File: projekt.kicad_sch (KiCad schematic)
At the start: 117 parts, among them IC1 DW01+G, IC4 MIC5504-3.3YM5-TR, J1 10118194-0001LF, J10 Conn_01x06_Pin, J2 TP4056, J4 Conn_01x02_Socket, Q1 AO3420, Q2 AO3420, Q3 AO3420, Q4 AO3420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

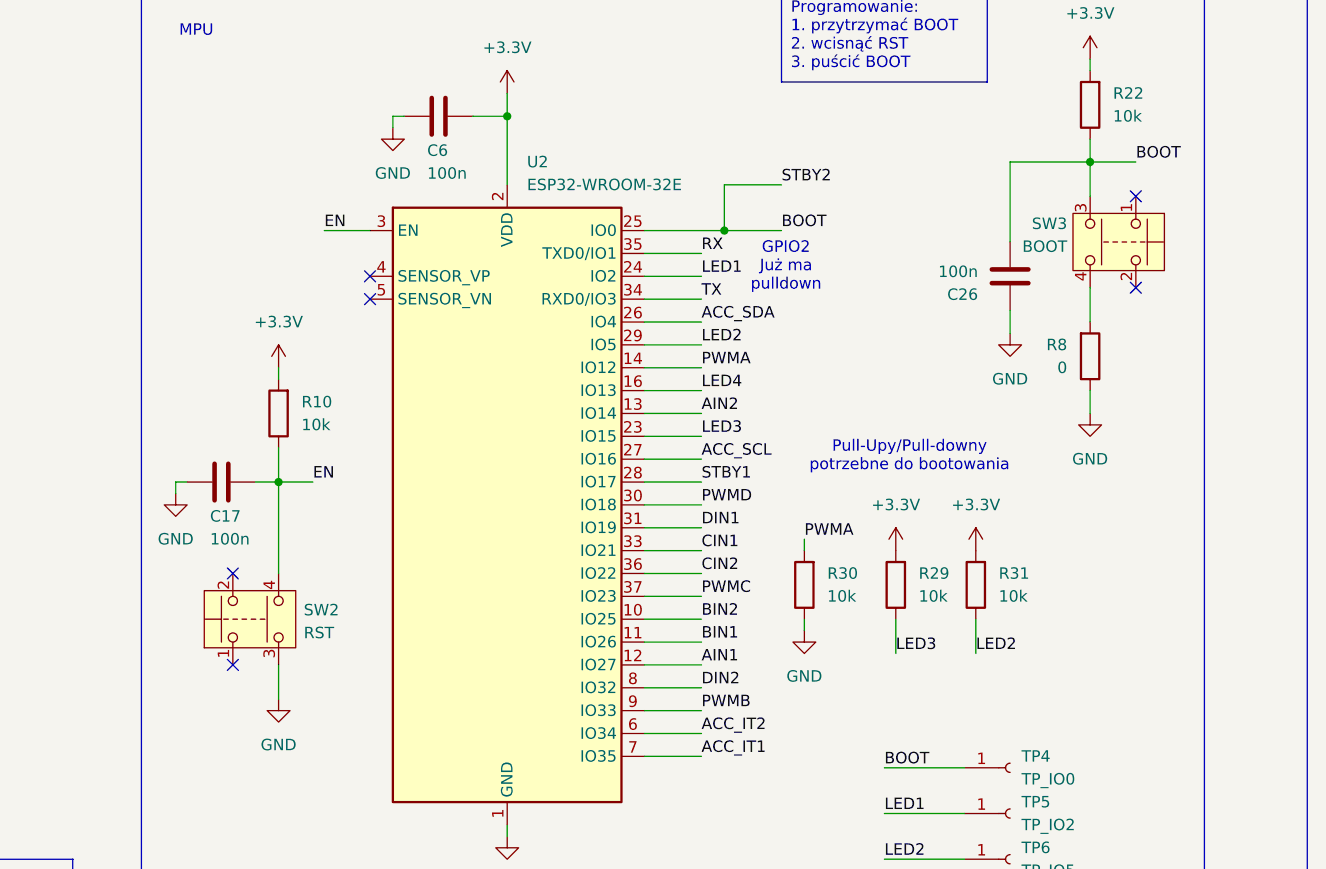
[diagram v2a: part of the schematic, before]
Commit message: Podmiana przycisków
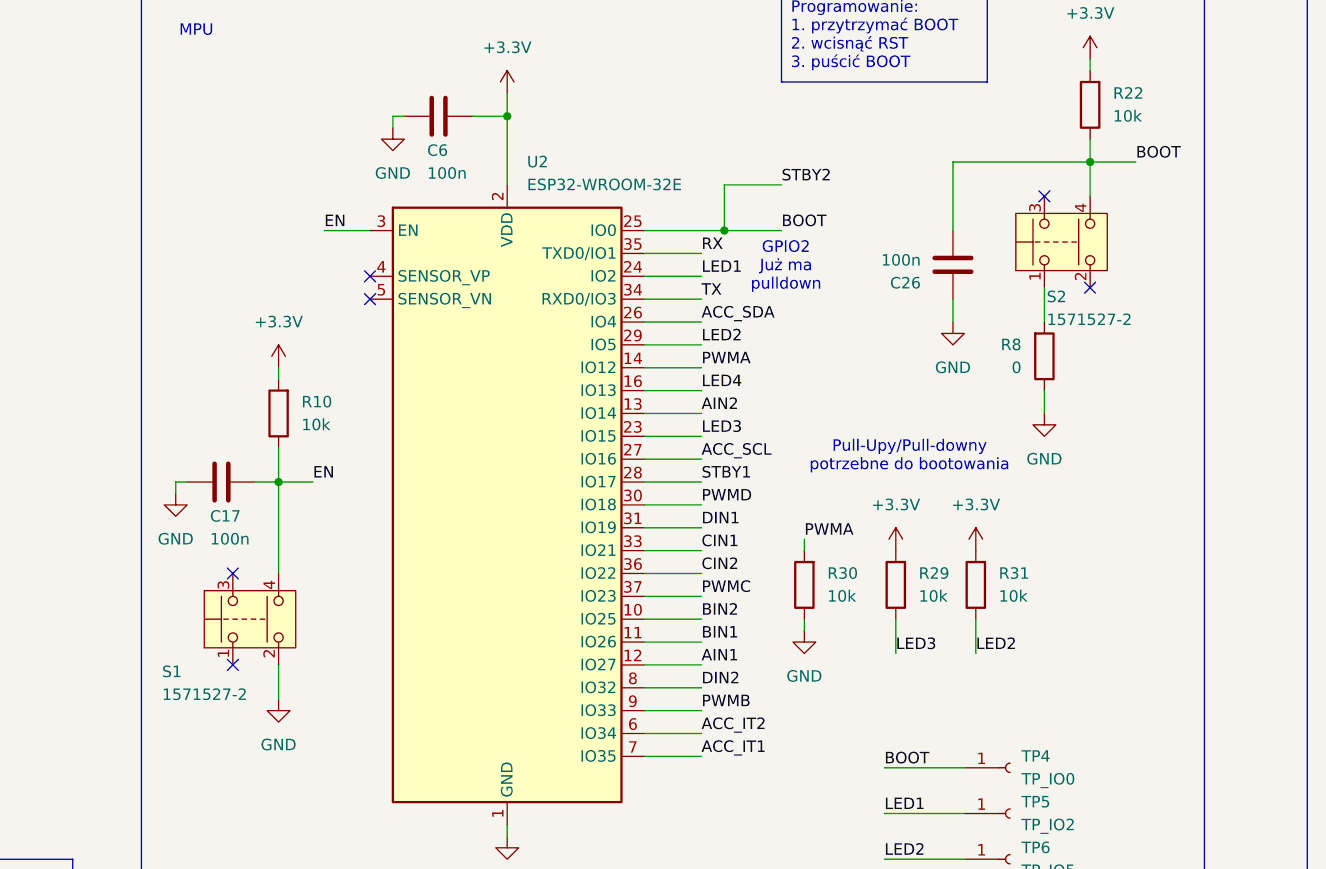
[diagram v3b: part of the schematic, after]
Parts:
- removed SW2: RST, Button_Switch_SMD:TSS 62 N, symbol Switch:SW_Push_Dual
- removed SW3: BOOT, Button_Switch_SMD:TSS 62 N, symbol Switch:SW_Push_Dual
- added S1, S2: 1571527-2, 15715272, symbol Switch:SW_Push_Dual
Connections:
- net BOOT: now also S2.4
- net EN: now also S1.4
- net GND: now also S1.2
- net at R8.2: now also S2.1
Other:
- moved on the sheet: C26, R8

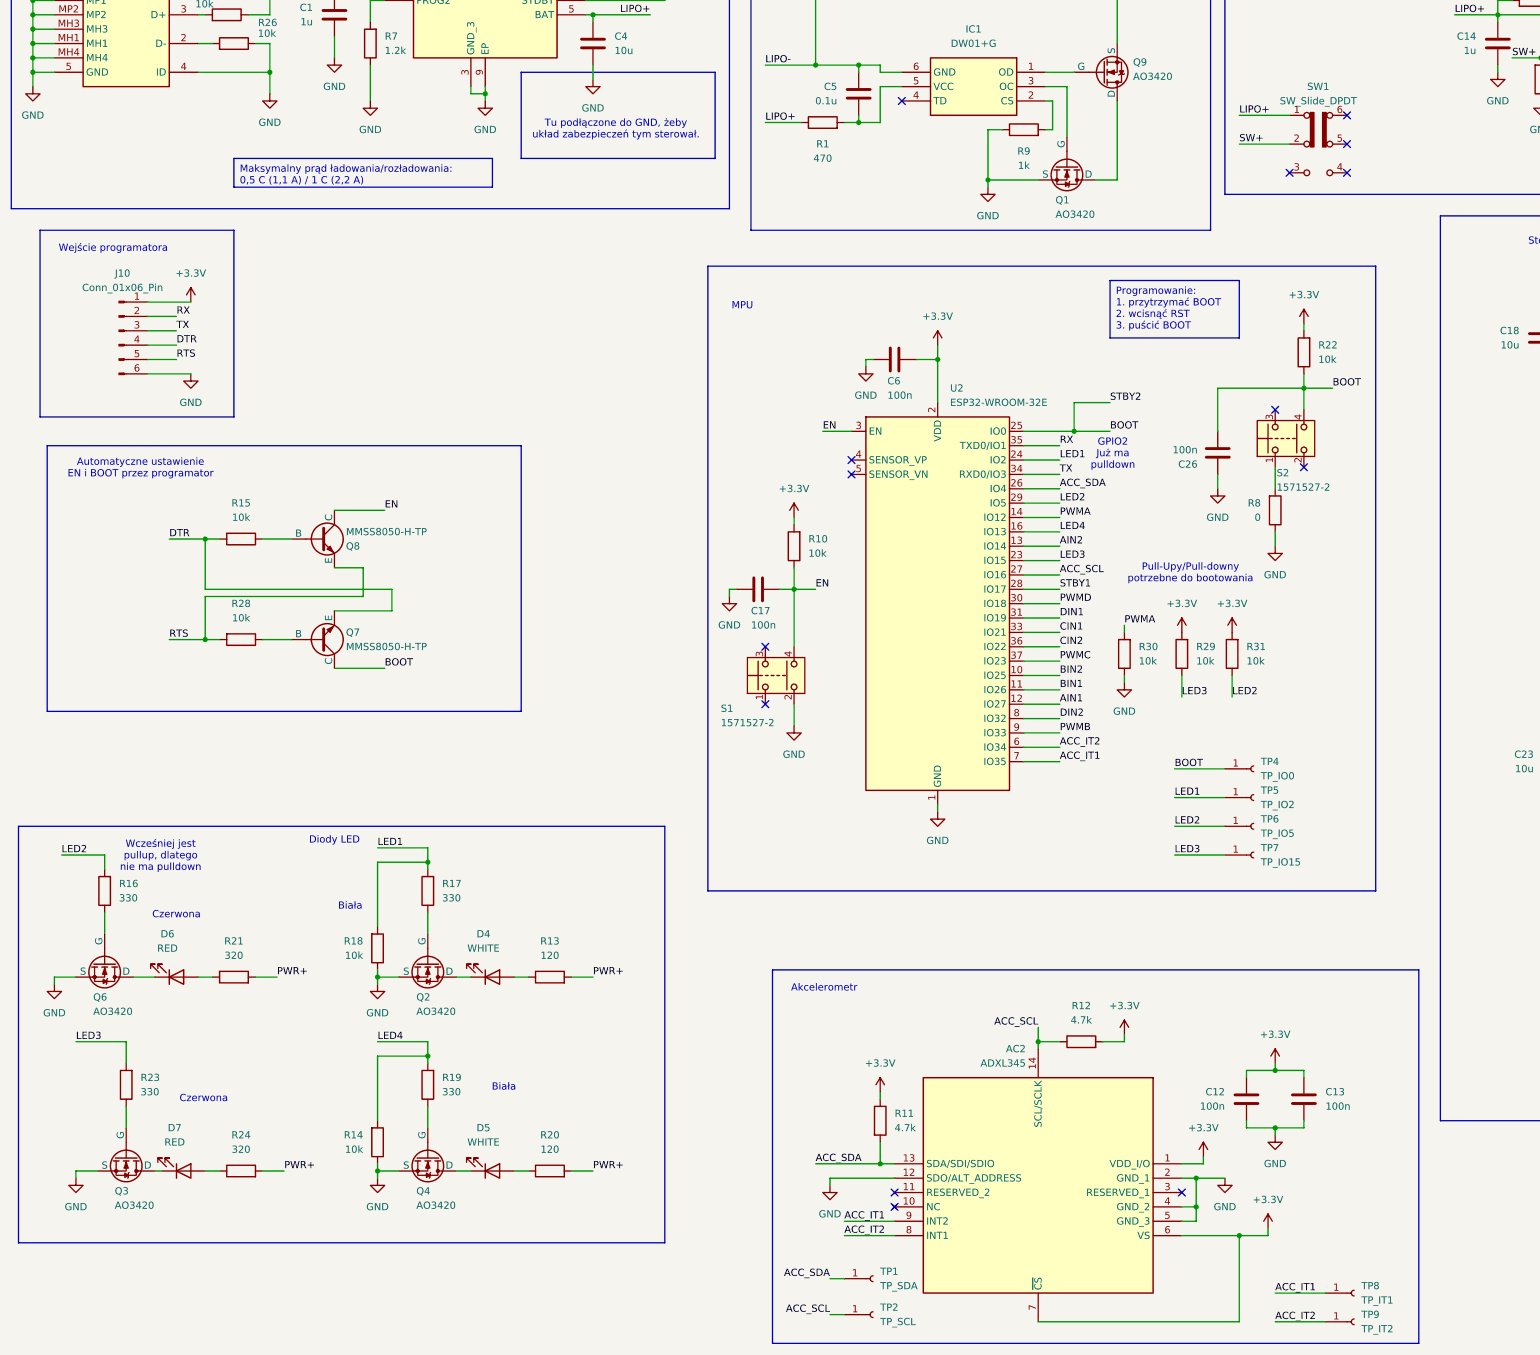
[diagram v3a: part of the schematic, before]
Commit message: Podmiana esp32 i footprinta switcha
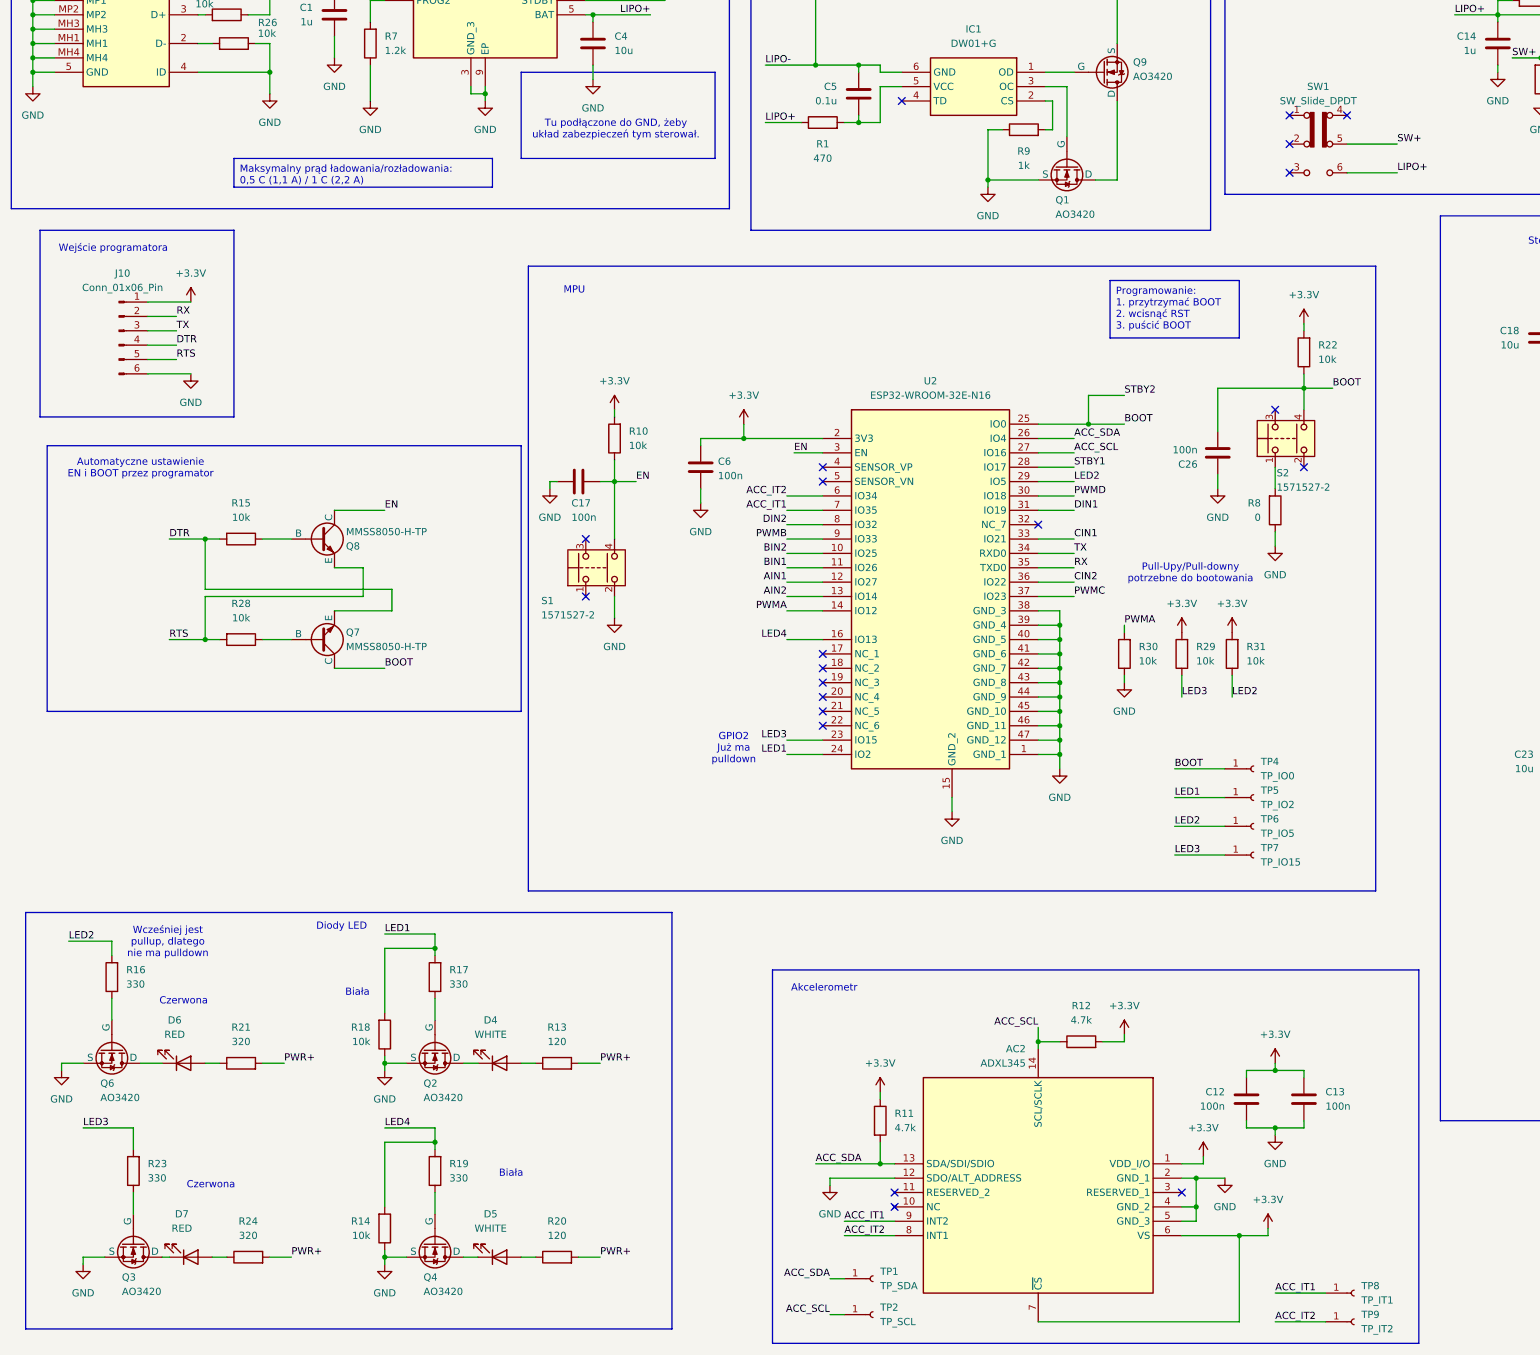
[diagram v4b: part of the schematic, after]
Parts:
- removed U2: ESP32-WROOM-32E, RF_Module:ESP32-WROOM-32D, symbol RF_Module:ESP32-WROOM-32E
- added U2: ESP32-WROOM-32E-N16, ESP32WROOM32EN16, symbol SamacSys_Parts:ESP32-WROOM-32E-N16
- SW1: footprint Button_Switch_THT:SW_CK_JS202011AQN_DPDT_Angled -> Button_Switch_THT:SS22T20
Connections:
- net +3.3V: now also U2.2 (3V3)
- net ACC_IT1: now also U2.7 (IO35)
- net ACC_IT2: now also U2.6 (IO34)
- net ACC_SCL: now also U2.27 (IO16)
- net ACC_SDA: now also U2.26 (IO4)
- net AIN1: now also U2.12 (IO27)
- net AIN2: now also U2.13 (IO14)
- net BIN1: now also U2.11 (IO26)
- net BIN2: now also U2.10 (IO25)
- net BOOT: now also U2.25 (IO0)
- net CIN1: now also U2.33 (IO21)
- net CIN2: now also U2.36 (IO22)
- net DIN1: now also U2.31 (IO19)
- net DIN2: now also U2.8 (IO32)
- net EN: now also U2.3 (EN)
- net GND: now also U2.1 (GND_1), U2.15 (GND_2), U2.38 (GND_3), U2.39 (GND_4), U2.40 (GND_5), U2.41 (GND_6), U2.42 (GND_7), U2.43 (GND_8), U2.44 (GND_9), U2.45 (GND_10), U2.46 (GND_11), U2.47 (GND_12)
- net LED1: now also U2.24 (IO2)
- net LED2: now also U2.29 (IO5)
- net LED3: now also U2.23 (IO15)
- net LED4: now also U2.16 (IO13)
- net LIPO+: now also SW1.6 (C); no longer SW1.1 (A)
- net PWMA: now also U2.14 (IO12)
- net PWMB: now also U2.9 (IO33)
- net PWMC: now also U2.37 (IO23)
- net PWMD: now also U2.30 (IO18)
- net RX: now also U2.35 (TXD0)
- net STBY1: now also U2.28 (IO17)
- net SW+: now also SW1.5 (B); no longer SW1.2 (B)
- net TX: now also U2.34 (RXD0)
- no-connect marks 15 -> 22
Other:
- moved on the sheet: C17, C6, D4, D5, D6, D7, Q2, Q3, Q4, Q6, R10, R13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

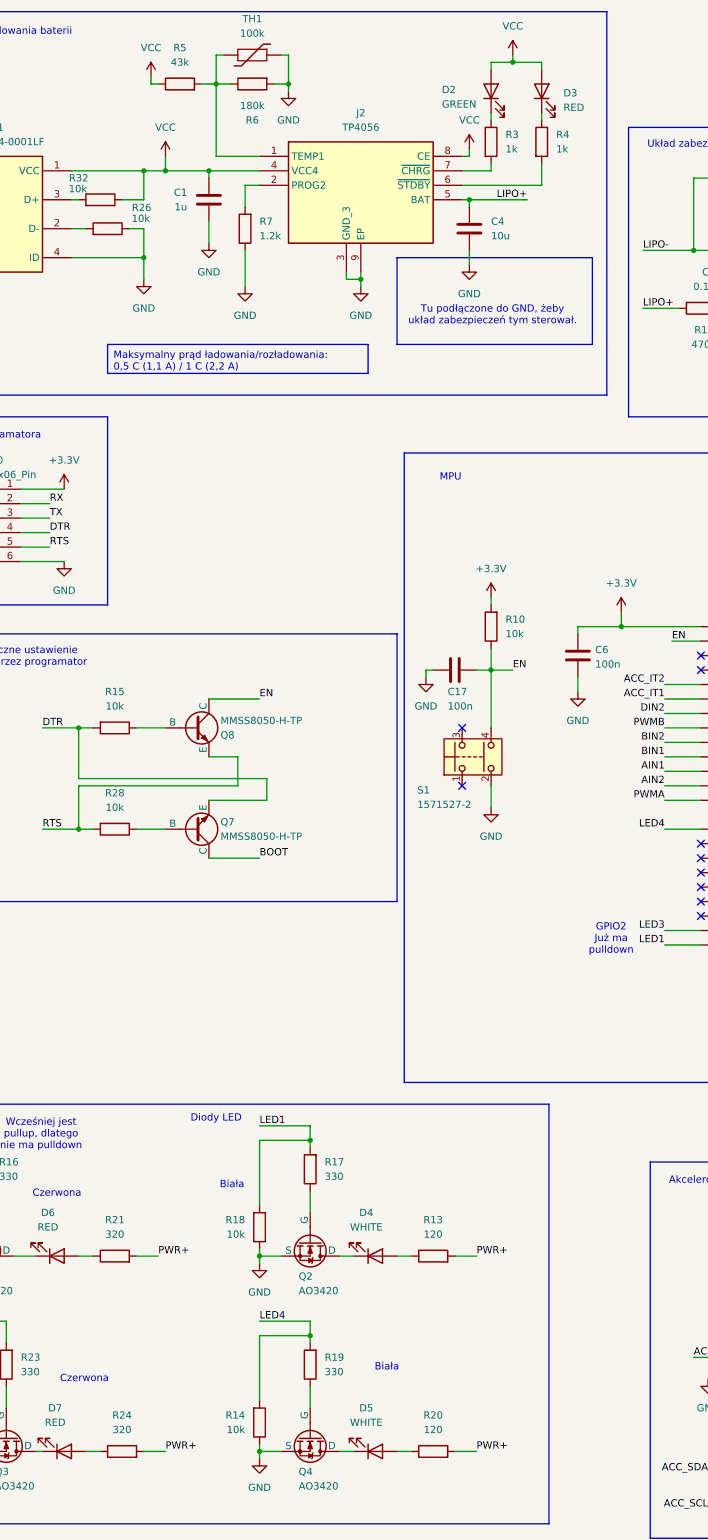
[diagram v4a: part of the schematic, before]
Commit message: Podmiana ścieżek na plane w dolnych wyjściach silników
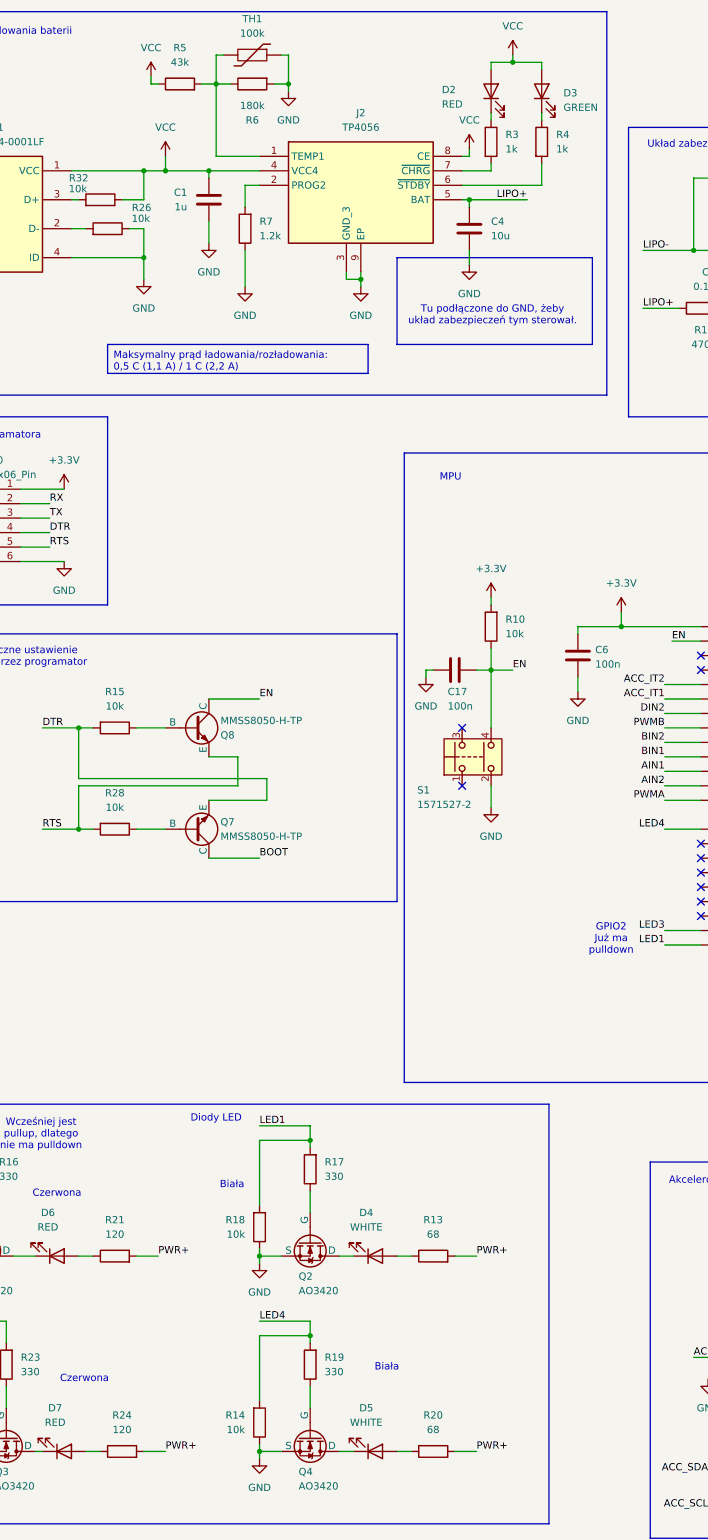
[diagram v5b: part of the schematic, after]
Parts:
- D2: value GREEN -> RED
- D3: value RED -> GREEN
- R13, R20: value 120 -> 68
- R21, R24: value 320 -> 120
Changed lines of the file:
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@@
 			)
 		)
-		(property "Value" "GREEN"
+		(property "Value" "RED"
 			(at 112.014 30.226 90)
 			(effects
@@
 			)
 		)
-		(property "Value" "120"
+		(property "Value" "68"
 			(at 110.49 262.89 90)
 			(effects
@@
 			)
 		)
-		(property "Value" "120"
+		(property "Value" "68"
 			(at 110.49 228.6 90)
 			(effects
@@
 			)
 		)
-		(property "Value" "RED"
+		(property "Value" "GREEN"
 			(at 133.35 30.7974 90)
 			(effects
@@
 			)
 		)
-		(property "Value" "320"
+		(property "Value" "120"
 			(at 54.61 228.6 90)
 			(effects
@@
 			)
 		)
-		(property "Value" "320"
+		(property "Value" "120"
 			(at 55.88 262.89 90)
 			(effects

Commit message: Przed wygenerowaniem gerberów
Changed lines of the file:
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@@
 	)
 	(junction
+		(at 50.8 157.48)
+		(diameter 0)
+		(color 0 0 0 0)
+	)
+	(junction
 		(at 17.78 49.53)
 		(diameter 0)
@@
 	)
 	(junction
-		(at 48.26 157.48)
-		(diameter 0)
-		(color 0 0 0 0)
-	)
-	(junction
 		(at 199.39 160.02)
 		(diameter 0)
@@
 	(wire
 		(pts
-			(xy 81.28 148.59) (xy 48.26 148.59)
+			(xy 71.12 149.86) (xy 48.26 149.86)
 		)
 		(stroke
@@
 	(wire
 		(pts
-			(xy 76.2 144.78) (xy 76.2 149.86)
+			(xy 71.12 144.78) (xy 71.12 146.05)
 		)
 		(stroke
@@
 	(wire
 		(pts
-			(xy 48.26 157.48) (xy 50.8 157.48)
-		)
-		(stroke
-			(width 0)
-			(type default)
-		)
-	)
-	(wire
-		(pts
 			(xy 284.48 109.22) (xy 297.18 109.22)
 		)
@@
 	(wire
 		(pts
-			(xy 48.26 149.86) (xy 48.26 157.48)
+			(xy 50.8 146.05) (xy 50.8 157.48)
 		)
 		(stroke
@@
 	(wire
 		(pts
-			(xy 81.28 152.4) (xy 71.12 152.4)
-		)
-		(stroke
-			(width 0)
-			(type default)
-		)
-	)
-	(wire
-		(pts
 			(xy 80.01 243.84) (xy 88.9 243.84)
 		)
@@
 	(wire
 		(pts
-			(xy 48.26 148.59) (xy 48.26 139.7)
+			(xy 48.26 149.86) (xy 48.26 139.7)
 		)
 		(stroke
@@
 	(wire
 		(pts
-			(xy 76.2 149.86) (xy 48.26 149.86)
+			(xy 71.12 146.05) (xy 50.8 146.05)
 		)
 		(stroke
@@
 	(wire
 		(pts
-			(xy 81.28 148.59) (xy 81.28 152.4)
+			(xy 71.12 149.86) (xy 71.12 152.4)
 		)
 		(stroke
@@
 	(wire
 		(pts
-			(xy 41.91 157.48) (xy 48.26 157.48)
+			(xy 41.91 157.48) (xy 50.8 157.48)
 		)
 		(stroke
@@
 		)
 		(stroke
-			(width 0)
-			(type default)
-		)
-	)
-	(wire
-		(pts
-			(xy 71.12 144.78) (xy 76.2 144.78)
-		)
-		(stroke

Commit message: Przed wygenerowaniem gerberów
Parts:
- SW1: value SW_Slide_DPDT -> SS22T20
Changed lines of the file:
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@@
 			)
 		)
-		(property "Value" "SW_Slide_DPDT"
+		(property "Value" "SS22T20"
 			(at 245.11 62.23 0)
 			(effects
